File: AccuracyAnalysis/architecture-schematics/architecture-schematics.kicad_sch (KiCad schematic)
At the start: 0 parts

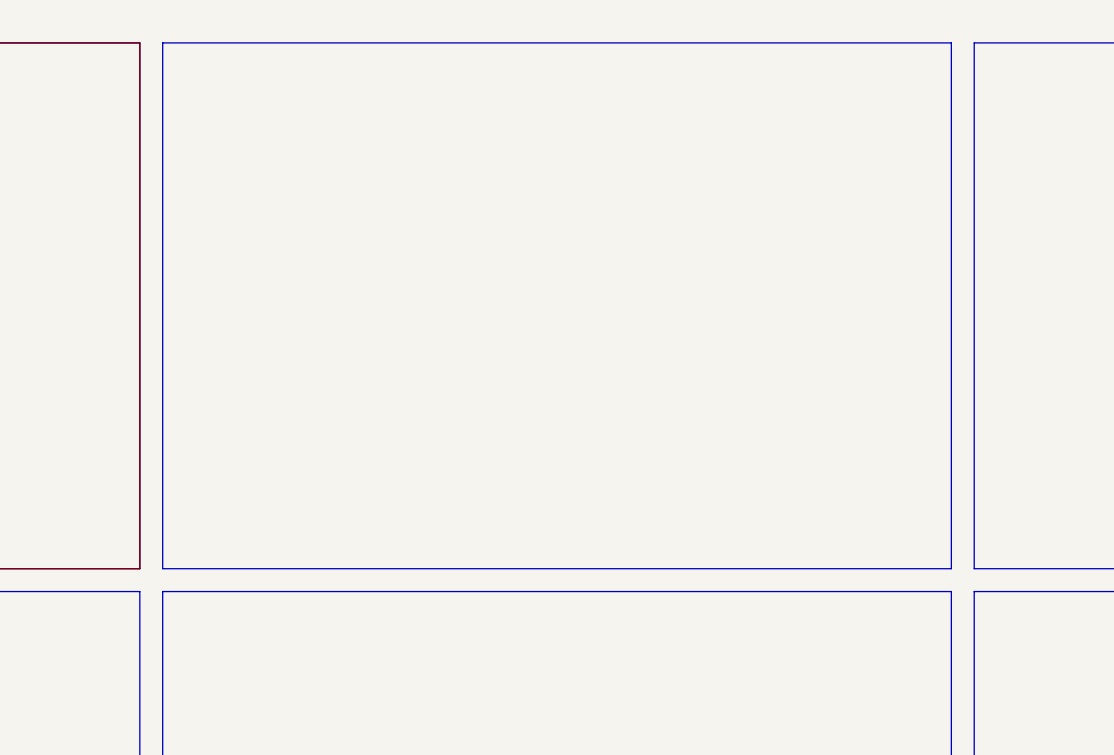
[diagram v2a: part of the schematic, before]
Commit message: add resistor-containing architecture
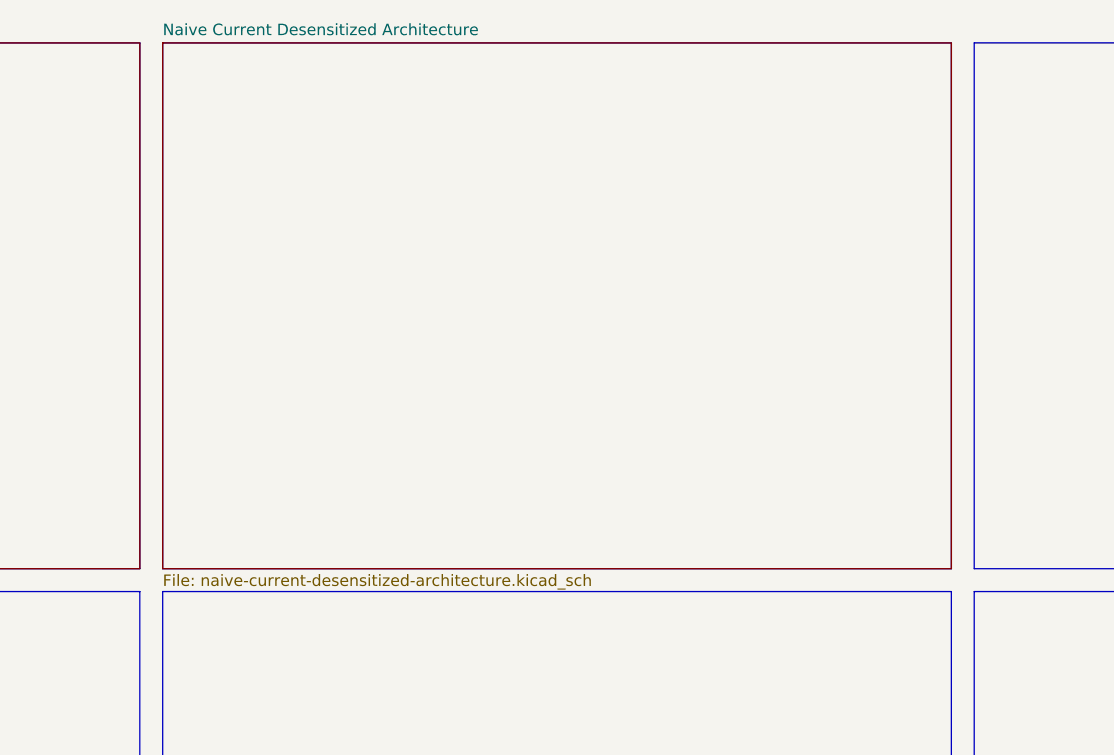
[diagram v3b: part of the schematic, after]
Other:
- added sheet Naive Current Desensitized Architecture (naive-current-desensitized-architecture.kicad_sch)
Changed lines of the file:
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@@
     (stroke (width 0) (type default) (color 0 0 0 0))
+  )
+  (sheet (at 104.14 13.97) (size 87.63 58.42) (fields_autoplaced)
+    (stroke (width 0.1524) (type solid) (color 0 0 0 0))
+    (fill (color 0 0 0 0.0000))
+    (property "Sheet name" "Naive Current Desensitized Architecture" (id 0) (at 104.14 13.2584 0)
+      (effects (font (size 1.27 1.27)) (justify left bottom))
+    )
+    (property "Sheet file" "naive-current-desensitized-architecture.kicad_sch" (id 1) (at 104.14 72.9746 0)
+      (effects (font (size 1.27 1.27)) (justify left top))
+    )
   )
   (sheet (at 13.97 13.97) (size 87.63 58.42) (fields_autoplaced)
@@
     (path "/" (page "1"))
     (path "/997b7e04-2ad8-4b2b-b19c-6c232748bb03" (page "2"))
+    (path "/2990165e-78a7-45c3-9269-a386bf551939" (page "3"))
   )
   (symbol_instances
@@
       (reference "#PWR?") (unit 1) (value "Earth") (footprint "")
     )
+    (path "/2990165e-78a7-45c3-9269-a386bf551939/0b7eed36-8f37-448c-98a6-e623bbdd1d37"
+      (reference "#PWR?") (unit 1) (value "Earth") (footprint "")
+    )
     (path "/997b7e04-2ad8-4b2b-b19c-6c232748bb03/1531f949-c0b1-46a2-b65a-2533148bd755"
+      (reference "#PWR?") (unit 1) (value "Earth") (footprint "")
+    )
+    (path "/2990165e-78a7-45c3-9269-a386bf551939/1531f949-c0b1-46a2-b65a-2533148bd755"
       (reference "#PWR?") (unit 1) (value "Earth") (footprint "")
     )
@@
       (reference "#PWR?") (unit 1) (value "Earth") (footprint "")
     )
+    (path "/2990165e-78a7-45c3-9269-a386bf551939/8daef6ac-8f87-4272-8463-1f1a9f8be54e"
+      (reference "#PWR?") (unit 1) (value "Earth") (footprint "")
+    )
     (path "/997b7e04-2ad8-4b2b-b19c-6c232748bb03/ad2e765e-c0db-47cb-b783-462d6881ee4c"
+      (reference "#PWR?") (unit 1) (value "Earth") (footprint "")
+    )
+    (path "/2990165e-78a7-45c3-9269-a386bf551939/ad2e765e-c0db-47cb-b783-462d6881ee4c"
       (reference "#PWR?") (unit 1) (value "Earth") (footprint "")
     )
@@
       (reference "#PWR?") (unit 1) (value "Earth") (footprint "")
     )
+    (path "/2990165e-78a7-45c3-9269-a386bf551939/eed56215-1ab5-4466-8b28-1d4d1efda5cf"
+      (reference "#PWR?") (unit 1) (value "Earth") (footprint "")
+    )
     (path "/997b7e04-2ad8-4b2b-b19c-6c232748bb03/02c0c6b2-0418-468b-bd64-2293078a00ec"
-      (reference "A0") (unit 1) (value "Arduino_UNO_R3") (footprint "Module:Arduino_UNO_R3")
+      (reference "A1") (unit 1) (value "Arduino_UNO_R3") (footprint "Module:Arduino_UNO_R3")
+    )
+    (path "/2990165e-78a7-45c3-9269-a386bf551939/02c0c6b2-0418-468b-bd64-2293078a00ec"
+      (reference "A2") (unit 1) (value "Arduino_UNO_R3") (footprint "Module:Arduino_UNO_R3")
     )
     (path "/997b7e04-2ad8-4b2b-b19c-6c232748bb03/7d4b5881-5b44-4eee-9597-5915739caf4b"
       (reference "BT1") (unit 1) (value "Battery_Cell") (footprint "")
     )
+    (path "/2990165e-78a7-45c3-9269-a386bf551939/7d4b5881-5b44-4eee-9597-5915739caf4b"
+      (reference "BT2") (unit 1) (value "Battery_Cell") (footprint "")
+    )
     (path "/997b7e04-2ad8-4b2b-b19c-6c232748bb03/58d11641-1522-42ac-a107-730ac47b6bea"
       (reference "D1") (unit 1) (value "DIODE") (footprint "")
     )
-    (path "/997b7e04-2ad8-4b2b-b19c-6c232748bb03/d3fc3360-ffa1-4769-b5ba-f6837dd1d2c3"
-      (reference "MES1") (unit 1) (value "Voltmeter_DIO") (footprint "")
+    (path "/2990165e-78a7-45c3-9269-a386bf551939/58d11641-1522-42ac-a107-730ac47b6bea"
+      (reference "D2") (unit 1) (value "DIODE") (footprint "")
     )
     (path "/997b7e04-2ad8-4b2b-b19c-6c232748bb03/6c0a5bf4-2acc-41a5-83d9-48e179906cd3"
-      (reference "MES2") (unit 1) (value "Ammeter_DIO") (footprint "")
+      (reference "MESA1") (unit 1) (value "Ammeter_DIO") (footprint "")
+    )
+    (path "/2990165e-78a7-45c3-9269-a386bf551939/6c0a5bf4-2acc-41a5-83d9-48e179906cd3"
+      (reference "MESA2") (unit 1) (value "Ammeter_DIO") (footprint "")
+    )
+    (path "/997b7e04-2ad8-4b2b-b19c-6c232748bb03/d3fc3360-ffa1-4769-b5ba-f6837dd1d2c3"
+      (reference "MESV1") (unit 1) (value "Voltmeter_DIO") (footprint "")
+    )
+    (path "/2990165e-78a7-45c3-9269-a386bf551939/d3fc3360-ffa1-4769-b5ba-f6837dd1d2c3"
+      (reference "MESV2") (unit 1) (value "Voltmeter_DIO") (footprint "")
     )
     (path "/997b7e04-2ad8-4b2b-b19c-6c232748bb03/7aca665c-4360-418d-ab13-83801d1d2549"
+      (reference "Q1") (unit 1) (value "Q_NMOS_GDS") (footprint "")
+    )
+    (path "/2990165e-78a7-45c3-9269-a386bf551939/7aca665c-4360-418d-ab13-83801d1d2549"
       (reference "Q2") (unit 1) (value "Q_NMOS_GDS") (footprint "")
     )
+    (path "/997b7e04-2ad8-4b2b-b19c-6c232748bb03/cf645ff9-6cea-4ed4-b081-fed77e09b77a"
+      (reference "RAdjCharge1") (unit 1) (value "digipot") (footprint "")
+    )
+    (path "/2990165e-78a7-45c3-9269-a386bf551939/cf645ff9-6cea-4ed4-b081-fed77e09b77a"
+      (reference "RAdjCharge2") (unit 1) (value "digipot") (footprint "")
+    )
     (path "/997b7e04-2ad8-4b2b-b19c-6c232748bb03/a61f526c-ecbc-4eb6-981f-f3db5b9ff351"
-      (reference "R1") (unit 1) (value "digipot") (footprint "")
+      (reference "RAdjDisch1") (unit 1) (value "digipot") (footprint "")
     )
-    (path "/997b7e04-2ad8-4b2b-b19c-6c232748bb03/cf645ff9-6cea-4ed4-b081-fed77e09b77a"
-      (reference "R2") (unit 1) (value "digipot") (footprint "")
+    (path "/2990165e-78a7-45c3-9269-a386bf551939/a61f526c-ecbc-4eb6-981f-f3db5b9ff351"
+      (reference "RAdjDisch2") (unit 1) (value "digipot") (footprint "")
+    )
+    (path "/2990165e-78a7-45c3-9269-a386bf551939/42d11911-9117-44f7-8a71-dabf9810d1af"
+      (reference "RDesen2") (unit 1) (value "R_US") (footprint "")
     )
     (path "/997b7e04-2ad8-4b2b-b19c-6c232748bb03/d76bdea3-97cc-4959-9685-e44670408d27"
-      (reference "R3") (unit 1) (value "R_US") (footprint "")
+      (reference "RfixedDiv2") (unit 1) (value "R_US") (footprint "")
+    )
+    (path "/2990165e-78a7-45c3-9269-a386bf551939/d76bdea3-97cc-4959-9685-e44670408d27"
+      (reference "RfixedDiv2") (unit 1) (value "R_US") (footprint "")
     )
     (path "/997b7e04-2ad8-4b2b-b19c-6c232748bb03/3097f818-ff13-4732-9d62-f32007c55fcf"
       (reference "U1") (unit 1) (value "Adjustable_LDO") (footprint "")
     )
+    (path "/2990165e-78a7-45c3-9269-a386bf551939/3097f818-ff13-4732-9d62-f32007c55fcf"
+      (reference "U2") (unit 1) (value "Adjustable_LDO") (footprint "")
+    )
   )
